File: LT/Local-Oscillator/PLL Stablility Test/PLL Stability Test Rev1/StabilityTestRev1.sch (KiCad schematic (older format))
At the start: 12 parts, among them J1 Conn_Coaxial, J11 Conn_Coaxial, J2 Conn_Coaxial, J6 Conn_01x02_Male, J9 Conn_01x03_Male, U3 LMH6611, U4 LMH6611

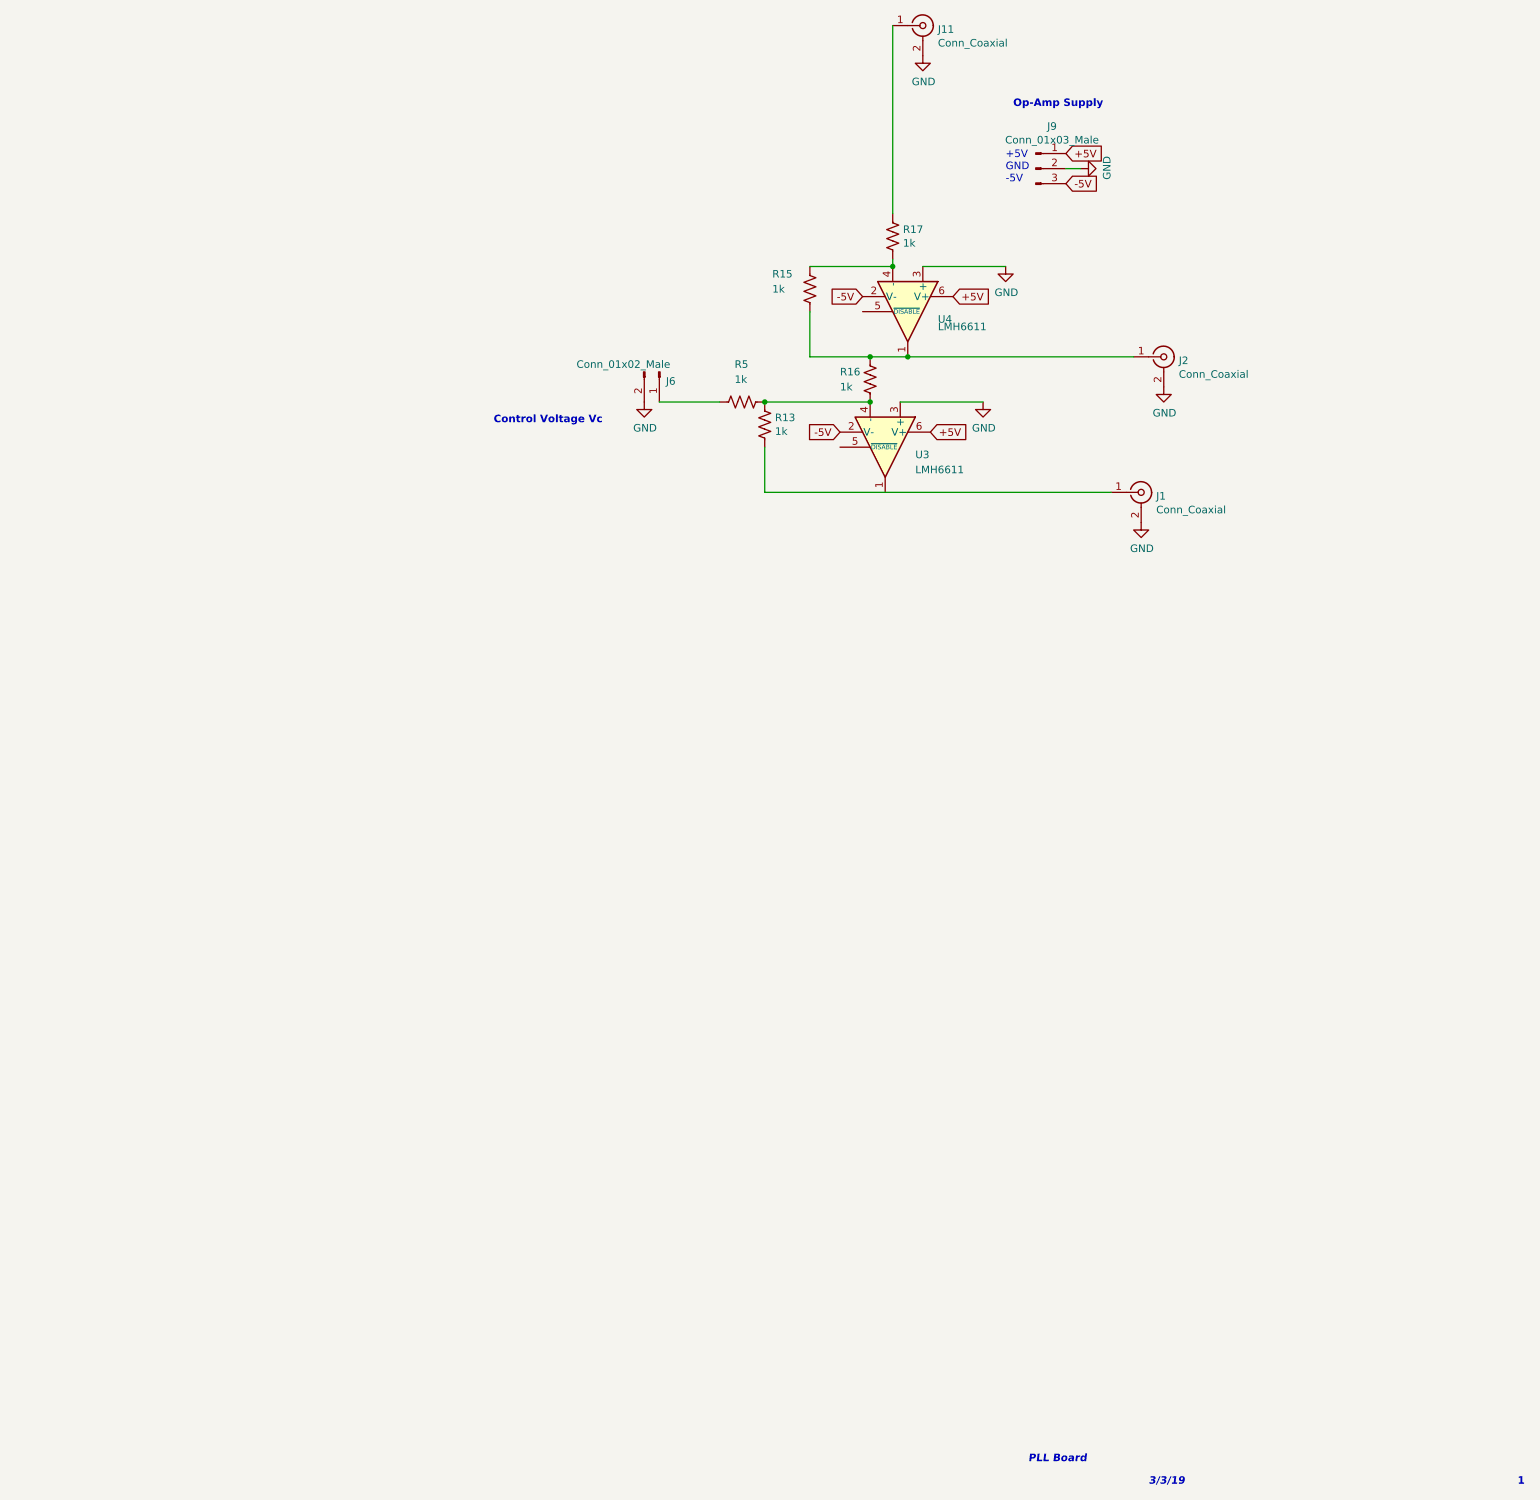
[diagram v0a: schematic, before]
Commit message: Added Capacitors to the Op-Amp board
I added some capacitors to the Op-Amp test board
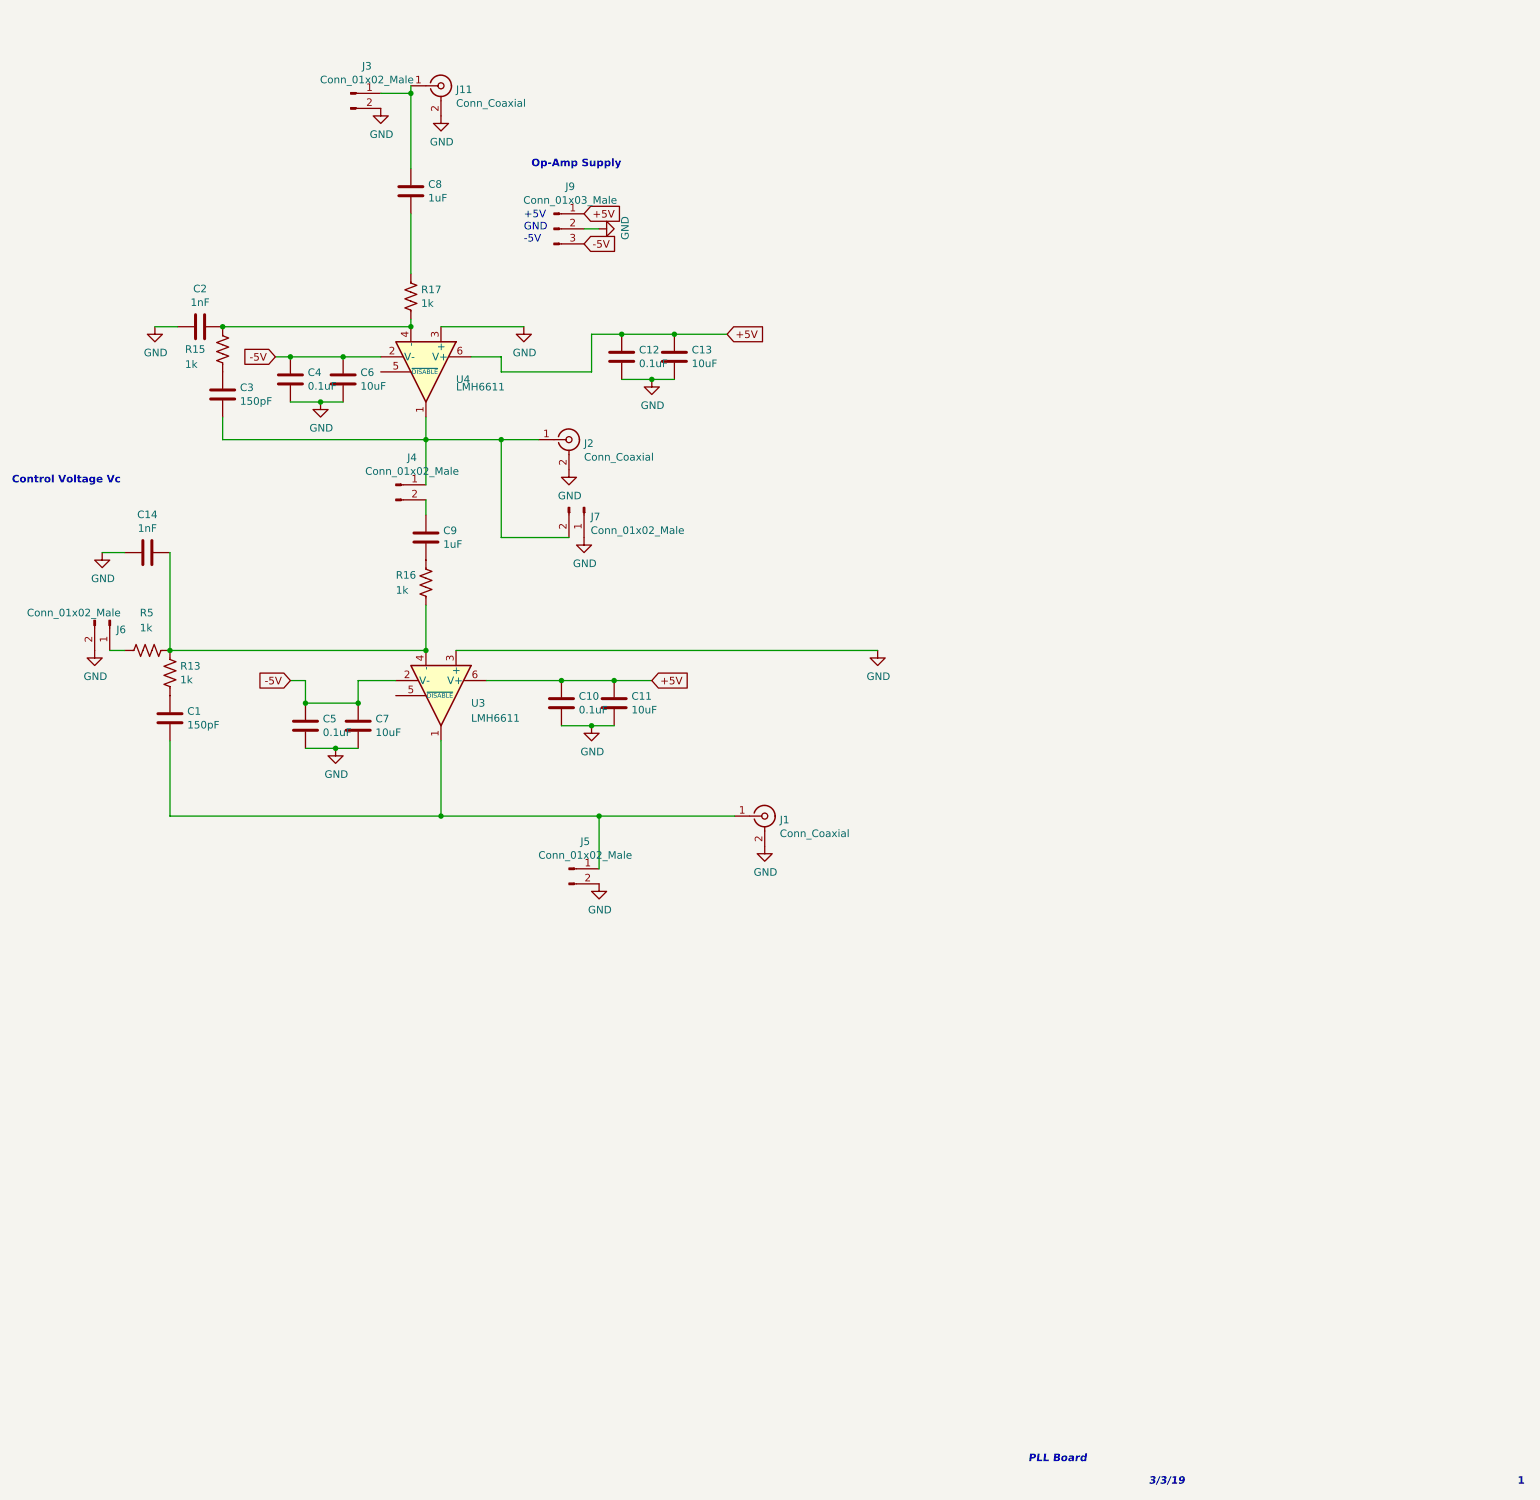
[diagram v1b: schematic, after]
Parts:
- added C1, C3: 150pF, Capacitor_SMD:C_0805_2012Metric_Pad1.15x1.40mm_HandSolder, symbol Device:C
- added C10, C12, C4, C5: 0.1uF, Capacitor_SMD:C_0805_2012Metric_Pad1.15x1.40mm_HandSolder, symbol Device:C
- added C11, C13, C6, C7: 10uF, Capacitor_SMD:C_0805_2012Metric_Pad1.15x1.40mm_HandSolder, symbol Device:C
- added C14, C2: 1nF, Capacitor_SMD:C_0805_2012Metric_Pad1.15x1.40mm_HandSolder, symbol Device:C
- added C8, C9: 1uF, Capacitor_SMD:C_0805_2012Metric_Pad1.15x1.40mm_HandSolder, symbol Device:C
- added J3, J4, J5, J7: Conn_01x02_Male, Connector_PinHeader_2.54mm:PinHeader_1x02_P2.54mm_Vertical, symbol Connector:Conn_01x02_Male
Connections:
- net +5V: now also C10.1, C11.1, C12.1, C13.1
- net -5V: now also C4.1, C5.1, C6.1, C7.1
- net GND: now also C10.2, C11.2, C12.2, C13.2, C14.2, C2.2, C4.2, C5.2, C6.2, C7.2, J3.2 (Pin_2), J5.2 (Pin_2), J7.1 (Pin_1)
- net at J2.1 (In), U4.1: now also C3.2, J4.1 (Pin_1), J7.2 (Pin_2); no longer R15.1, R16.1
- net at R15.2, R17.2, U4.4 (-): now also C2.1
- net at J1.1 (In), U3.1: now also C1.2, J5.1 (Pin_1); no longer R13.2
- net at R13.1, R16.2, R5.1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: now also C14.1
- net at R17.1: now also C8.2; no longer J11.1 (In)
- new net: C3.1, R15.1
- new net: C8.1, J11.1 (In), J3.1 (Pin_1)
- new net: C1.1, R13.2
- new net: C9.2, R16.1
- new net: C9.1, J4.2 (Pin_2)
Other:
- moved on the sheet: J1, J11, J2, J6, J9, R13, R15, R16, R17, R5, U3, U4
